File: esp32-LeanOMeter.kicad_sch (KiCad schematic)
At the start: 4 parts, among them J1 Conn_01x06-SdCard, J2 Conn_02x15_Counter_Clockwise, J3 Conn_01x04-GpsModuleNeoM8N, J4 Conn_01x10-BNO085

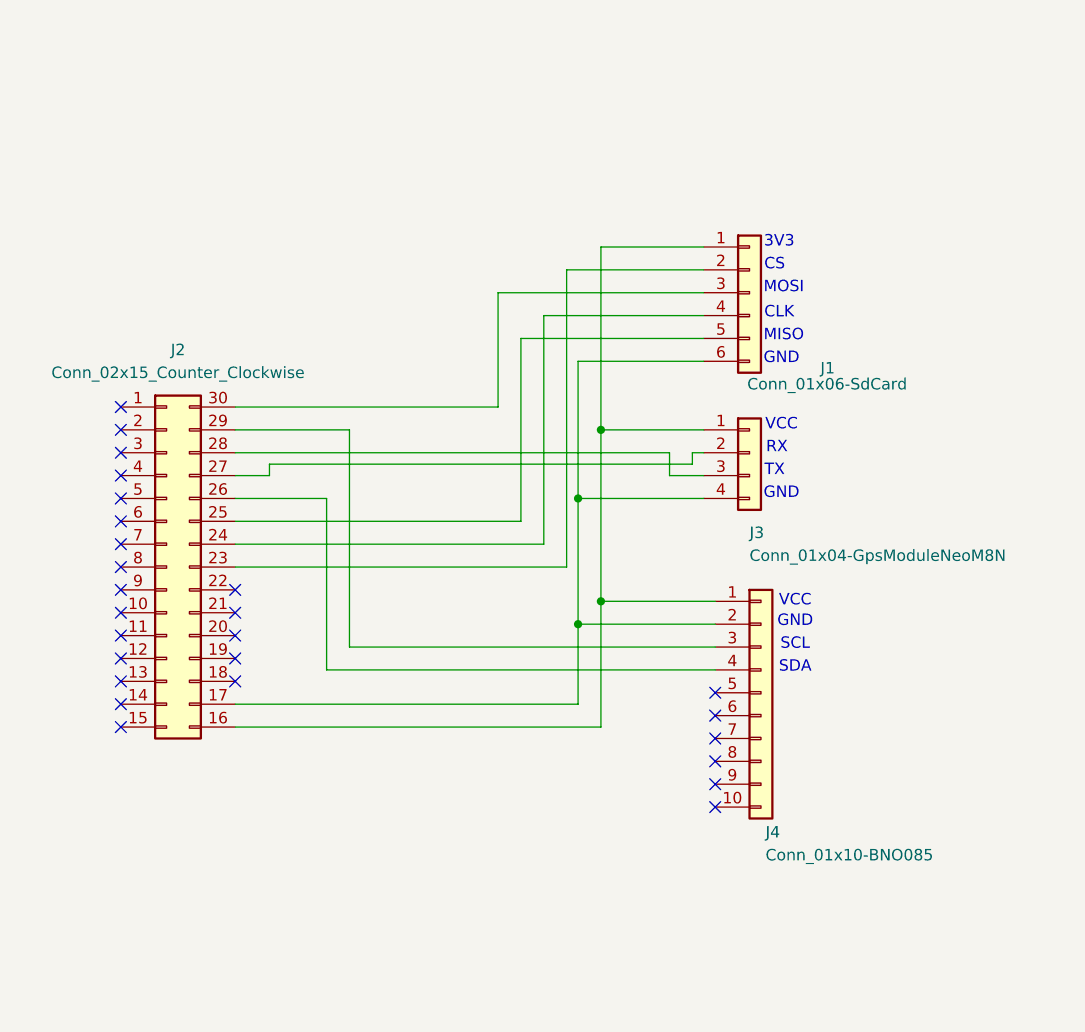
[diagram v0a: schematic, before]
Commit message: updated rx and tx values
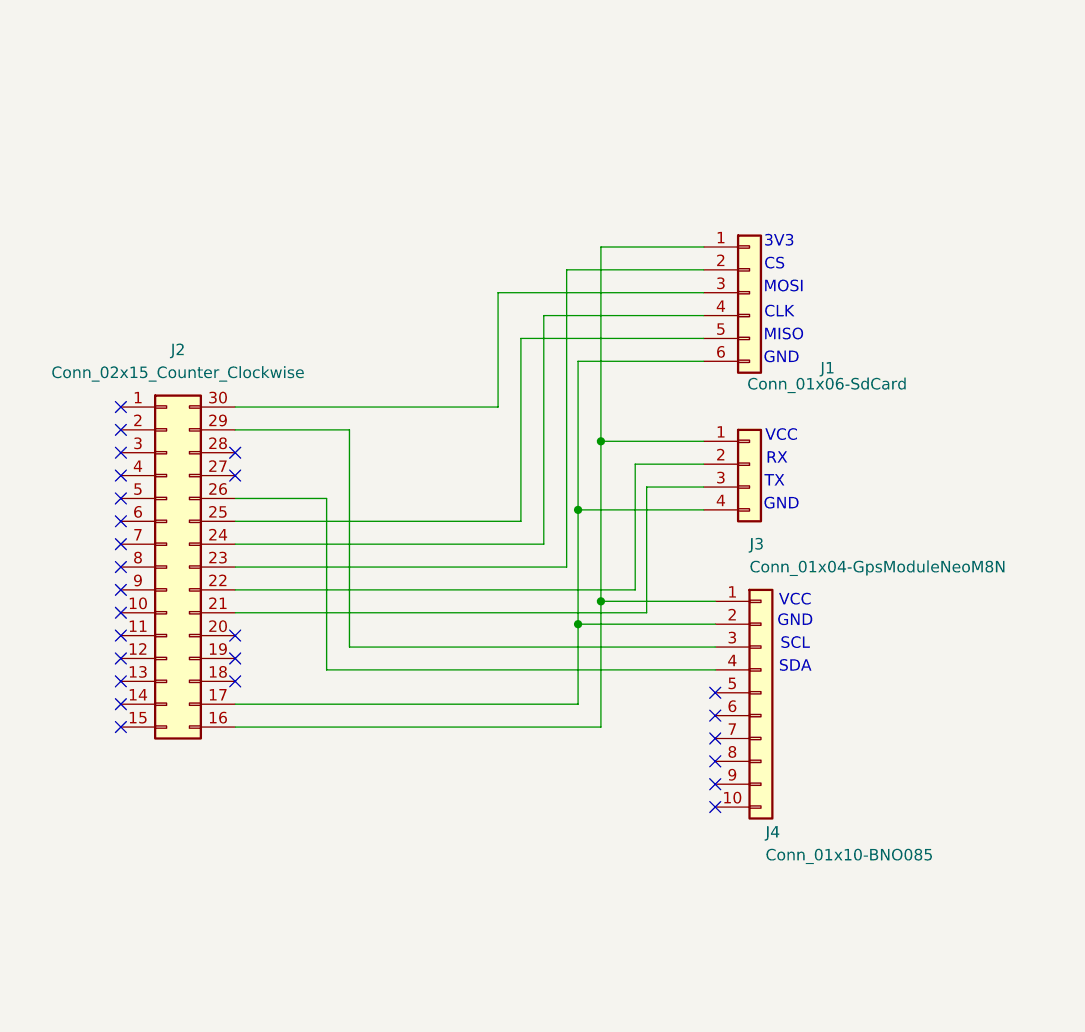
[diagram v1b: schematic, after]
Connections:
- net at J2.21 (Pin_21): now also J3.3 (Pin_3)
- net at J2.22 (Pin_22): now also J3.2 (Pin_2)
- net at J2.27 (Pin_27): no longer J3.2 (Pin_2)
- net at J2.28 (Pin_28): no longer J3.3 (Pin_3)
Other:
- moved on the sheet: J3
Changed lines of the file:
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@@
 	(text "GND"
 		(exclude_from_sim no)
-		(at 205.486 93.472 0)
+		(at 205.486 94.742 0)
 		(effects
 			(font
@@
 	(text "TX"
 		(exclude_from_sim no)
-		(at 204.724 90.932 0)
+		(at 204.724 92.202 0)
 		(effects
 			(font
@@
 	(text "RX"
 		(exclude_from_sim no)
-		(at 204.978 88.392 0)
+		(at 204.978 89.662 0)
 		(effects
 			(font
@@
 	(text "VCC"
 		(exclude_from_sim no)
-		(at 205.486 85.852 0)
+		(at 205.486 87.122 0)
 		(effects
 			(font
@@
 	)
 	(junction
-		(at 182.88 93.98)
+		(at 182.88 95.25)
 		(diameter 0)
 		(color 0 0 0 0)
 	)
 	(junction
-		(at 185.42 86.36)
+		(at 185.42 87.63)
 		(diameter 0)
 		(color 0 0 0 0)
@@
 	)
 	(no_connect
+		(at 144.78 88.9)
+	)
+	(no_connect
 		(at 132.08 88.9)
 	)
@@
 	)
 	(no_connect
-		(at 144.78 104.14)
+		(at 144.78 91.44)
 	)
 	(no_connect
@@
 	)
 	(no_connect
-		(at 144.78 106.68)
-	)
-	(no_connect
 		(at 144.78 114.3)
 	)
@@
 	(wire
 		(pts
-			(xy 185.42 86.36) (xy 196.85 86.36)
-		)
-		(stroke
-			(width 0)
-			(type default)
-			(color 245 23 255 1)
-		)
-	)
-	(wire
-		(pts
-			(xy 182.88 93.98) (xy 196.85 93.98)
-		)
-		(stroke
-			(width 0)
-			(type default)
-			(color 245 23 255 1)
+			(xy 185.42 87.63) (xy 196.85 87.63)
+		)
+		(stroke
+			(width 0)
+			(type default)
+			(color 255 0 2 1)
 		)
 	)
@@
 	(wire
 		(pts
+			(xy 185.42 87.63) (xy 185.42 105.41)
+		)
+		(stroke
+			(width 0)
+			(type default)
+		)
+	)
+	(wire
+		(pts
 			(xy 144.78 101.6) (xy 181.61 101.6)
 		)
@@
 	(wire
 		(pts
-			(xy 185.42 86.36) (xy 185.42 66.04)
-		)
-		(stroke
-			(width 0)
-			(type default)
-		)
-	)
-	(wire
-		(pts
 			(xy 144.78 96.52) (xy 176.53 96.52)
 		)
@@
 	(wire
 		(pts
-			(xy 182.88 93.98) (xy 182.88 78.74)
-		)
-		(stroke
-			(width 0)
-			(type default)
+			(xy 182.88 78.74) (xy 182.88 95.25)
+		)
+		(stroke
+			(width 0)
+			(type default)
+		)
+	)
+	(wire
+		(pts
+			(xy 196.85 90.17) (xy 189.23 90.17)
+		)
+		(stroke
+			(width 0)
+			(type default)
+			(color 255 0 2 1)
 		)
 	)
@@
 	(wire
 		(pts
-			(xy 196.85 88.9) (xy 195.58 88.9)
-		)
-		(stroke
-			(width 0)
-			(type default)
-			(color 245 23 255 1)
-		)
-	)
-	(wire
-		(pts
-			(xy 182.88 93.98) (xy 182.88 107.95)
-		)
-		(stroke
-			(width 0)
-			(type default)
-		)
-	)
-	(wire
-		(pts
 			(xy 157.48 110.49) (xy 157.48 86.36)
 		)
@@
 	(wire
 		(pts
-			(xy 148.59 90.17) (xy 148.59 91.44)
-		)
-		(stroke
-			(width 0)
-			(type default)
-			(color 245 23 255 1)
-		)
-	)
-	(wire
-		(pts
 			(xy 173.99 83.82) (xy 173.99 71.12)
 		)
@@
 	(wire
 		(pts
-			(xy 193.04 91.44) (xy 196.85 91.44)
-		)
-		(stroke
-			(width 0)
-			(type default)
-			(color 245 23 255 1)
+			(xy 190.5 106.68) (xy 190.5 92.71)
+		)
+		(stroke
+			(width 0)
+			(type default)
+			(color 255 0 2 1)
+		)
+	)
+	(wire
+		(pts
+			(xy 144.78 106.68) (xy 190.5 106.68)
+		)
+		(stroke
+			(width 0)
+			(type default)
+			(color 255 0 2 1)
+		)
+	)
+	(wire
+		(pts
+			(xy 189.23 90.17) (xy 189.23 104.14)
+		)
+		(stroke
+			(width 0)
+			(type default)
+			(color 255 0 2 1)
 		)
 	)
@@
 	(wire
 		(pts
+			(xy 189.23 104.14) (xy 144.78 104.14)
+		)
+		(stroke
+			(width 0)
+			(type default)
+			(color 255 0 2 1)
+		)
+	)
+	(wire
+		(pts
 			(xy 144.78 119.38) (xy 185.42 119.38)
 		)
@@
 	(wire
 		(pts
-			(xy 148.59 91.44) (xy 144.78 91.44)
-		)
-		(stroke
-			(width 0)
-			(type default)
-			(color 245 23 255 1)
+			(xy 190.5 92.71) (xy 196.85 92.71)
+		)
+		(stroke
+			(width 0)
+			(type default)
+			(color 255 0 2 1)
+		)
+	)
+	(wire
+		(pts
+			(xy 182.88 95.25) (xy 182.88 107.95)
+		)
+		(stroke
+			(width 0)
+			(type default)
 		)
 	)
@@
 	(wire
 		(pts
-			(xy 195.58 90.17) (xy 148.59 90.17)
-		)
-		(stroke
-			(width 0)
-			(type default)
-			(color 245 23 255 1)
-		)
-	)
-	(wire
-		(pts
-			(xy 195.58 88.9) (xy 195.58 90.17)
-		)
-		(stroke
-			(width 0)
-			(type default)
-			(color 245 23 255 1)
+			(xy 182.88 95.25) (xy 196.85 95.25)
+		)
+		(stroke
+			(width 0)
+			(type default)
+			(color 255 0 2 1)
 		)
 	)
@@
 	(wire
 		(pts
-			(xy 144.78 88.9) (xy 193.04 88.9)
-		)
-		(stroke
-			(width 0)
-			(type default)
-			(color 245 23 255 1)
-		)
-	)
-	(wire
-		(pts
-			(xy 193.04 88.9) (xy 193.04 91.44)
-		)
-		(stroke
-			(width 0)
-			(type default)
-			(color 245 23 255 1)
-		)
-	)
-	(wire
-		(pts
 			(xy 198.12 110.49) (xy 157.48 110.49)
 		)
@@
 	(wire
 		(pts
-			(xy 185.42 86.36) (xy 185.42 105.41)
+			(xy 185.42 66.04) (xy 185.42 87.63)
 		)
 		(stroke
@@
 	(symbol
 		(lib_id "Connector_Generic:Conn_01x04")
-		(at 201.93 88.9 0)
+		(at 201.93 90.17 0)
 		(unit 1)
 		(body_style 1)
@@
 		(dnp no)
 		(property "Reference" "J3"
-			(at 201.93 97.79 0)
+			(at 201.93 99.06 0)
 			(show_name no)
 			(do_not_autoplace no)
@@
 		)
 		(property "Value" "Conn_01x04-GpsModuleNeoM8N"
-			(at 201.93 100.33 0)
+			(at 201.93 101.6 0)
 			(show_name no)
 			(do_not_autoplace no)
@@
 		)
 		(property "Footprint" "Connector_PinHeader_2.54mm:PinHeader_1x04_P2.54mm_Vertical"
-			(at 201.93 88.9 0)
+			(at 201.93 90.17 0)
 			(hide yes)
 			(show_name no)
@@
 		)
 		(property "Datasheet" ""
-			(at 201.93 88.9 0)
+			(at 201.93 90.17 0)
 			(hide yes)
 			(show_name no)
@@
 		)
 		(property "Description" "Generic connector, single row, 01x04, script generated (kicad-library-utils/schlib/autogen/connector/)"
-			(at 201.93 88.9 0)
-			(hide yes)
-			(show_name no)
+			(at 201.93 90.17 0)
+			(hide yes)
+			(show_name no)

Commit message: fix: changed the gps module. added resistors, added capacitors
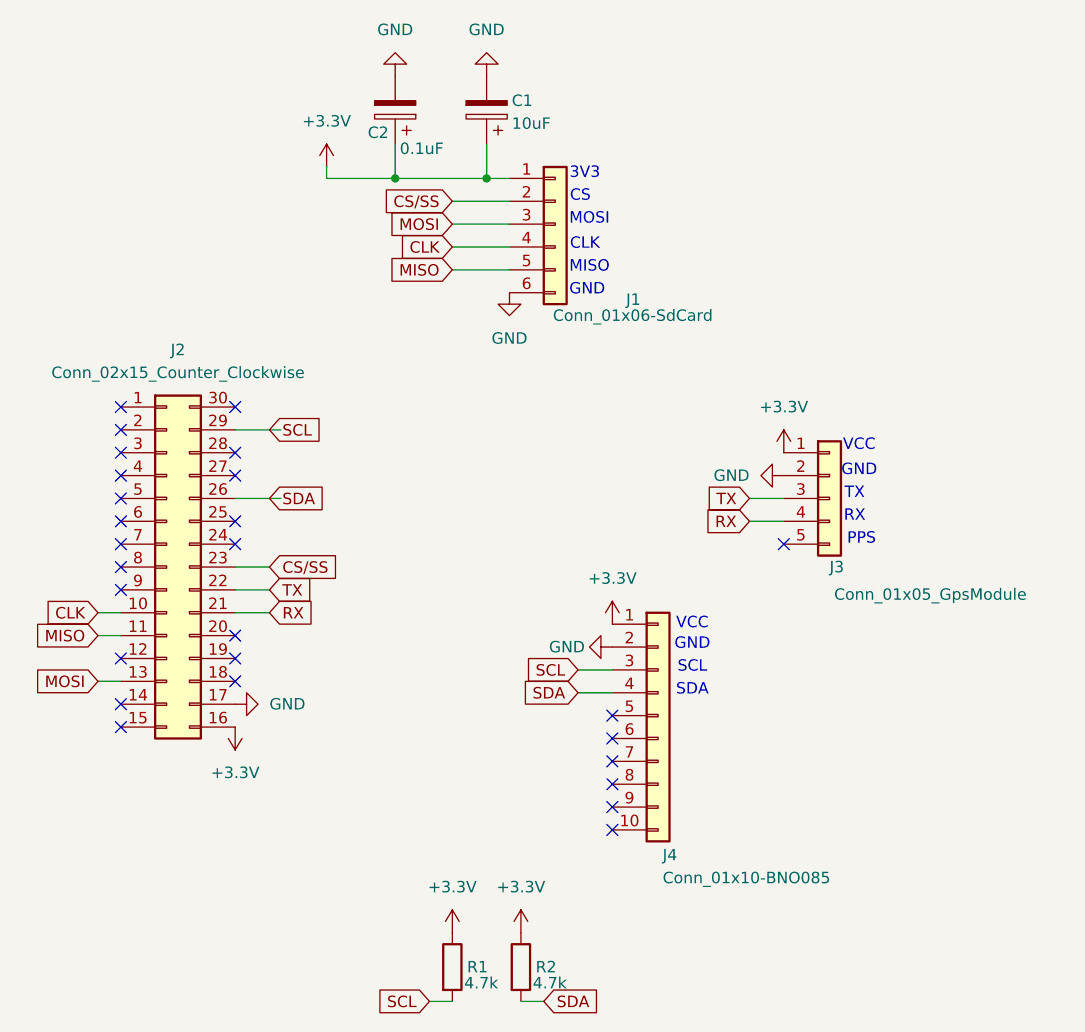
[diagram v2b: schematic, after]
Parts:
- removed J3: Conn_01x04-GpsModuleNeoM8N, Connector_PinHeader_2.54mm:PinHeader_1x04_P2.54mm_Vertical, symbol Connector_Generic:Conn_01x04
- added C1: 10uF, Capacitor_THT:CP_Radial_D5.0mm_P2.00mm, symbol Device:C_Polarized
- added C2: 0.1uF, Capacitor_THT:CP_Radial_D4.0mm_P1.50mm, symbol Device:C_Polarized
- added J3: Conn_01x05_GpsModule, Connector_PinHeader_2.54mm:PinHeader_1x05_P2.54mm_Vertical, symbol Connector_Generic:Conn_01x05
- added R1, R2: 4.7k, Resistor_THT:R_Axial_DIN0207_L6.3mm_D2.5mm_P7.62mm_Horizontal, symbol Device:R
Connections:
- net +3.3V: now reaches J1.1 (Pin_1), J2.16 (Pin_16), J4.1 (Pin_1)
- net +3.3V: now also C1.1, C2.1, J3.1 (Pin_1), R1.1, R2.1
- net GND: now reaches J1.6 (Pin_6), J2.17 (Pin_17), J4.2 (Pin_2)
- net GND: now also C1.2, C2.2, J3.2 (Pin_2)
- net SCL: now reaches J2.29 (Pin_29), J4.3 (Pin_3)
- net SCL: now also R1.2
- net SDA: now reaches J2.26 (Pin_26), J4.4 (Pin_4)
- net SDA: now also R2.2
- net CS/SS: now reaches J1.2 (Pin_2), J2.23 (Pin_23)
- net at J2.30 (Pin_30): no longer J1.3 (Pin_3)
- net at J2.24 (Pin_24): no longer J1.4 (Pin_4)
- net at J2.25 (Pin_25): no longer J1.5 (Pin_5)
- net CLK: now reaches J2.10 (Pin_10)
- net CLK: now also J1.4 (Pin_4)
- net MISO: now reaches J2.11 (Pin_11)
- net MISO: now also J1.5 (Pin_5)
- net MOSI: now reaches J2.13 (Pin_13)
- net MOSI: now also J1.3 (Pin_3)
- net RX: now reaches J2.21 (Pin_21)
- net RX: now also J3.4 (Pin_4)
- net TX: now reaches J2.22 (Pin_22)
- net TX: now also J3.3 (Pin_3)
- no-connect marks 26 -> 27
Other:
- note added: "PPS"
- moved on the sheet: J1, J4
